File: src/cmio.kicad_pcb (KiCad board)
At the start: 2 copper layers, 7 parts, among them J1 CONN_02X20, J3 CM3Lite, J4 CONN_COAXIAL, J5 CONN_02X20, SW1 SW_Push

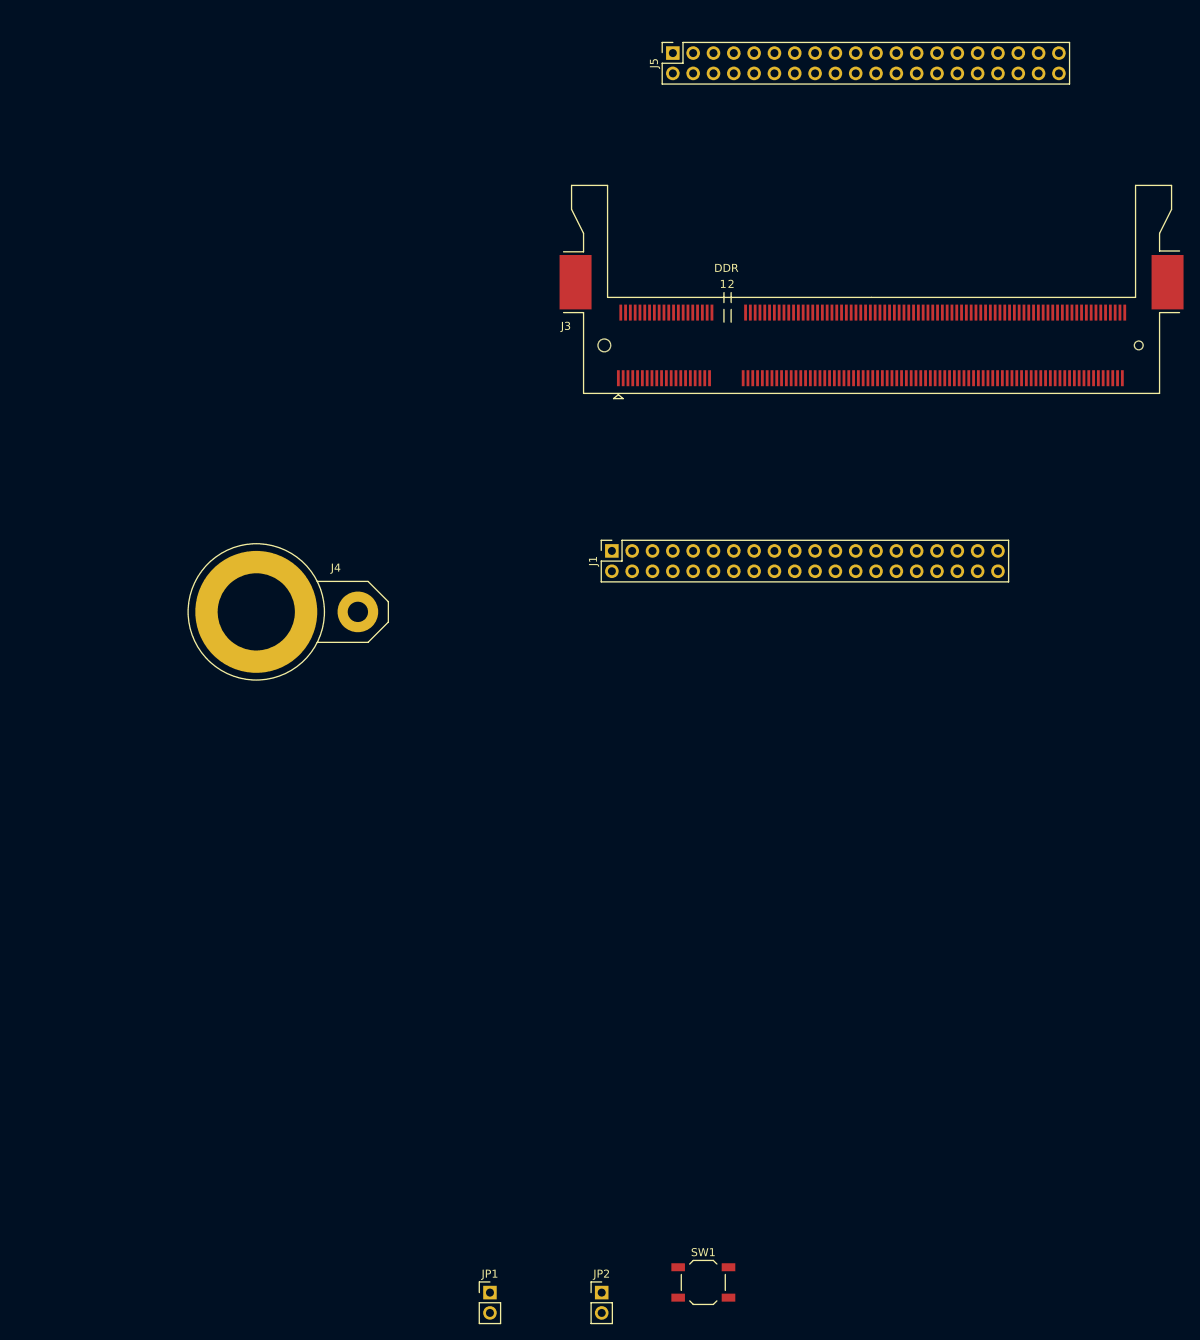
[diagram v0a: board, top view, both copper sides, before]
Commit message: Add Micro SD Card Footprint and 20-TQFP
Signed-off-by: Mahyar Koshkouei <deltabeard@users.noreply.github.com>
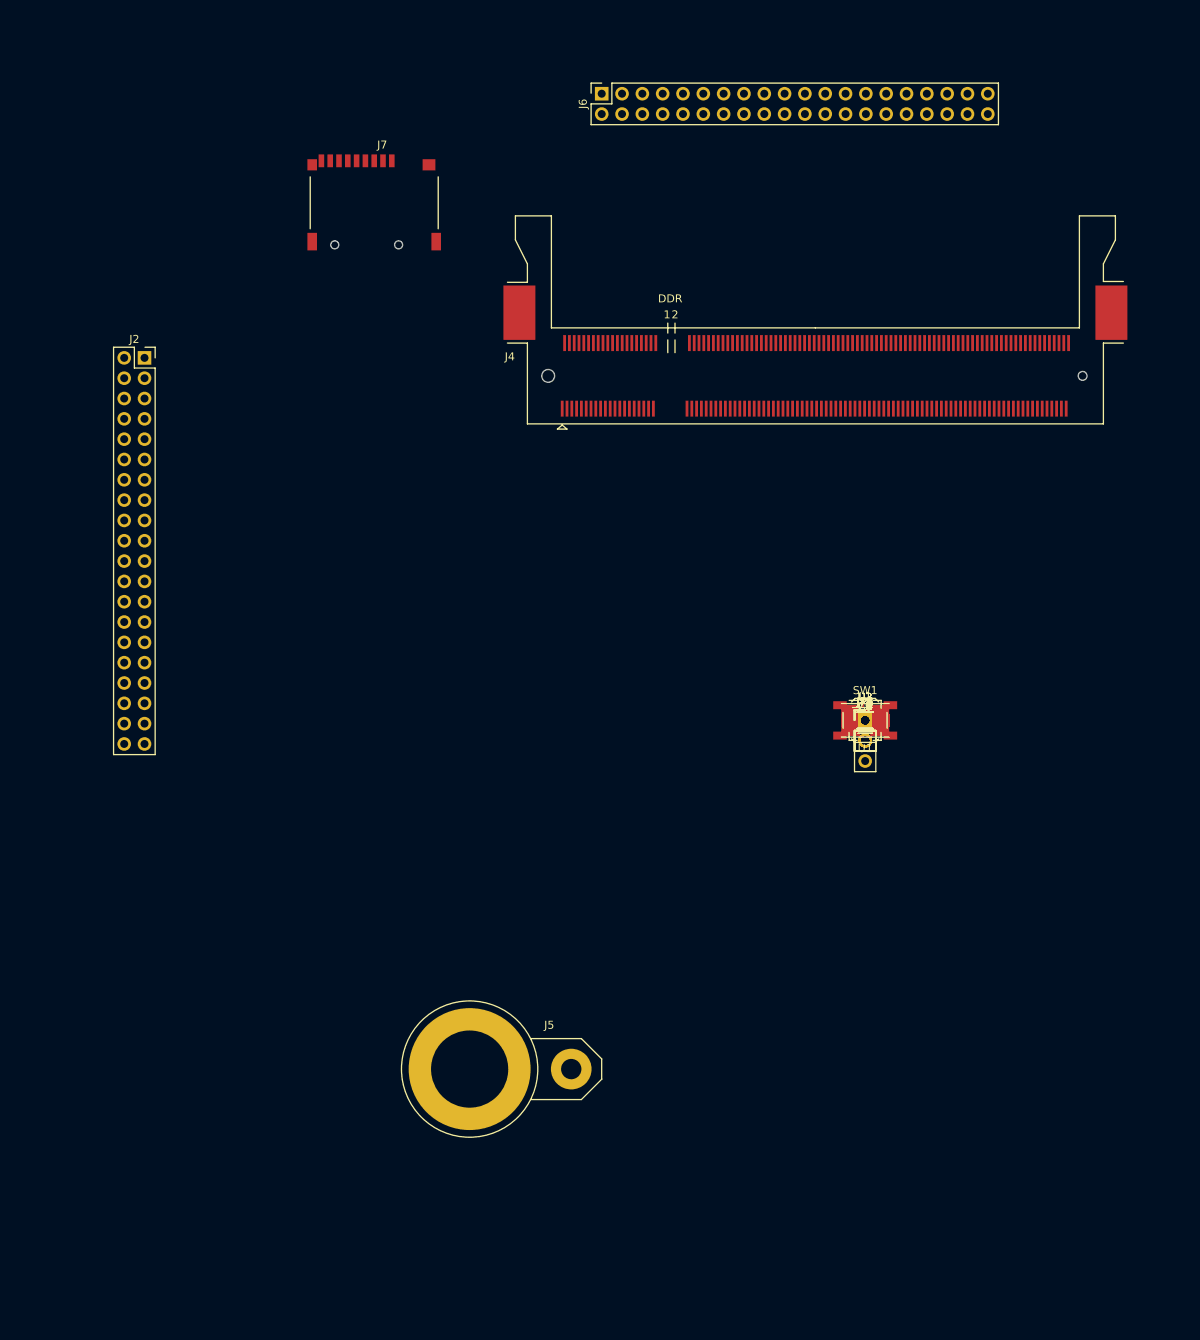
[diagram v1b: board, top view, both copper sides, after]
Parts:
- removed J3: CM3Lite, Sockets:Socket_SODIMM_DDR1-2_TE_1612618
- added C1, C2, C7, C8: 1uF, Capacitors_SMD:C_1206_HandSoldering, F.Cu at (148.5, 105.0)
- added C3, C6, C9: 22uF, Capacitors_SMD:C_1206_HandSoldering, F.Cu at (148.5, 105.0)
- added C4, C5: 10nF, Capacitors_SMD:C_1206_HandSoldering, F.Cu at (148.5, 105.0)
- added J2: CONN_02X20, Socket_Strips:Socket_Strip_Straight_2x20_Pitch2.54mm, F.Cu at (58.4, 59.7)
- added J6: CONN_02X20, Socket_Strips:Socket_Strip_Straight_2x20_Pitch2.54mm, F.Cu at (115.6, 26.7)
- added J7: Micro_SD_Card_TFP09_2_12B, foot:TFP09-2-12B, F.Cu at (87.1, 35.6)
- added JP3: 3.3 OUT, Pin_Headers:Pin_Header_Straight_1x02_Pitch2.54mm, F.Cu at (148.5, 105.0)
- added JP4: EN_Jumper, Socket_Strips:Socket_Strip_Straight_1x03_Pitch2.54mm, F.Cu at (148.5, 105.0)
- added JP5: TP, Pin_Headers:Pin_Header_Straight_1x02_Pitch2.54mm, F.Cu at (148.5, 105.0)
- added JP6: Disable SD Card, Pin_Headers:Pin_Header_Straight_1x02_Pitch2.54mm, F.Cu at (148.5, 105.0)
- added L1: 1uH, Inductors:Inductor_Taiyo-Yuden_NR-40xx_HandSoldering, F.Cu at (148.5, 105.0)
- added U1: ISL91107IR, foot:20_TQFP, F.Cu at (148.5, 105.0)
- added U2: LD3985M18R, TO_SOT_Packages_SMD:SOT-23-5, F.Cu at (148.5, 105.0)
- added U3: LD3985M28R, TO_SOT_Packages_SMD:SOT-23-5, F.Cu at (148.5, 105.0)
- J1: value CONN_02X20 -> CONN_01X02_MALE; footprint Socket_Strips:Socket_Strip_Straight_2x20_Pitch2.54mm -> Pin_Headers:Pin_Header_Straight_1x02_Pitch2.54mm
- J4: value CONN_COAXIAL -> CM3Lite; footprint Connect:BNC -> Sockets:Socket_SODIMM_DDR1-2_TE_1612618
- J5: value CONN_02X20 -> CONN_COAXIAL; footprint Socket_Strips:Socket_Strip_Straight_2x20_Pitch2.54mm -> Connect:BNC
- JP1: value TP -> 1V8 LDO IN
- JP2: value Disable SD Card -> 2V8 LDO IN
- moved J5 127.6 mm to (111.8, 148.6), turned to 0 degrees
- moved JP1 85.5 mm to (148.5, 105.0)
- moved JP2 78.7 mm to (148.5, 105.0)
- moved SW1 73.1 mm to (148.5, 105.0)
- moved J4 64.4 mm to (142.3, 61.9)
- moved J1 38.1 mm to (148.5, 105.0), turned to 0 degrees
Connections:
- J1 pad 2: +5V -> +3V3
- J4 pad 1: TVDAC -> GND
- J4 pad 2: GND -> Net-(J4-Pad2)
- J5 pad 1: +3V3 -> TVDAC
- J5 pad 2: +5V -> GND
- JP1 pad 1: (no net) -> +5V
- JP1 pad 2: +5V -> Net-(C1-Pad1)
- JP2 pad 1: Net-(J3-Pad2) -> +5V
- JP2 pad 2: GND -> Net-(C2-Pad1)
- SW1 pad 2: Net-(J3-Pad177) -> Net-(J4-Pad177)

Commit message: Before removing RPi GPIO Compat
Signed-off-by: Mahyar Koshkouei <deltabeard@users.noreply.github.com>
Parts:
- added J3: USB_OTG, foot:Micro_USB_B_10104110, F.Cu at (69.3, 24.0)
- added J8: CONN_01X06, Pin_Headers:Pin_Header_Straight_1x06_Pitch2.54mm, F.Cu at (66.0, 59.1)
- J4: footprint Sockets:Socket_SODIMM_DDR1-2_TE_1612618 -> foot:CM3_LeftDrillHole_Socket_SODIMM_DDR1-2_TE_1612618; moved to B.Cu
- J5: footprint Connect:BNC -> foot:RCA_PHONO
- moved JP4 133.2 mm to (45.7, 20.3), turned to 90 degrees
- moved JP3 131.6 mm to (45.7, 22.9), turned to 90 degrees
- moved JP5 129.6 mm to (45.7, 26.0), turned to 90 degrees
- moved JP1 128.1 mm to (45.7, 28.5), turned to 90 degrees
- moved JP2 126.6 mm to (45.7, 31.1), turned to 90 degrees
- moved J1 125.1 mm to (45.7, 33.6), turned to 90 degrees
- moved C2 112.7 mm to (57.0, 39.2), turned to 90 degrees
- moved L1 112.6 mm to (64.5, 30.0), turned to 270 degrees
- moved C8 111.6 mm to (61.8, 34.8)
- moved U3 110.1 mm to (60.2, 39.2)
- moved U1 109.1 mm to (69.6, 29.7)
- moved C5 106.9 mm to (64.0, 39.5), turned to 90 degrees
- moved C6 106.1 mm to (74.0, 29.5), turned to 90 degrees
- moved C3 105.1 mm to (71.0, 34.0)
- moved C9 104.3 mm to (76.5, 29.5), turned to 90 degrees
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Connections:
- J4 pad 165: (no net) -> /D+
- J4 pad 167: (no net) -> /D-
- J4 pad 168: (no net) -> OTDIG
- J6 pad 28: /DSI0_0 -> +5V
- J6 pad 30: /DSI0_1 -> +3V3
- J6 pad 32: /DSI0_2 -> +2V8
- J6 pad 34: /DSI0_3 -> +1V8
- J6 pad 36: /DSI0_4 -> GND
- J6 pad 38: /DSI0_5 -> GND
- JP5 pad 1: (no net) -> Net-(J3-Pad1)
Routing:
- net /D+: track 0.00 -> 47.4 mm, vias 0 -> 1
- net /D-: track 0.00 -> 47.1 mm, vias 0 -> 1
- net OTDIG: track 0.00 -> 42.9 mm, vias 0 -> 1
- net GND: track 0.00 -> 32.5 mm, vias 0 -> 3
- net G1: track 0.00 -> 31.4 mm
- net TVDAC: track 0.00 -> 25.7 mm
- net Net-(J3-Pad1): track 0.00 -> 24.6 mm, vias 0 -> 1
- net R1: track 0.00 -> 22.9 mm
- net G4: track 0.00 -> 22.1 mm
- net R0: track 0.00 -> 21.1 mm
- net G0: track 0.00 -> 20.6 mm
- net /DSI0_5: track 0.00 -> 20.6 mm
- net /DSI0_4: track 0.00 -> 18.1 mm
- net /DSI0_3: track 0.00 -> 17.1 mm
- net /DSI0_2: track 0.00 -> 14.8 mm
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- added copper zone on B.Cu, net GND
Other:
- board outline added: 89 x 51 mm
- rule via_min_size: 0.4 -> 0.5

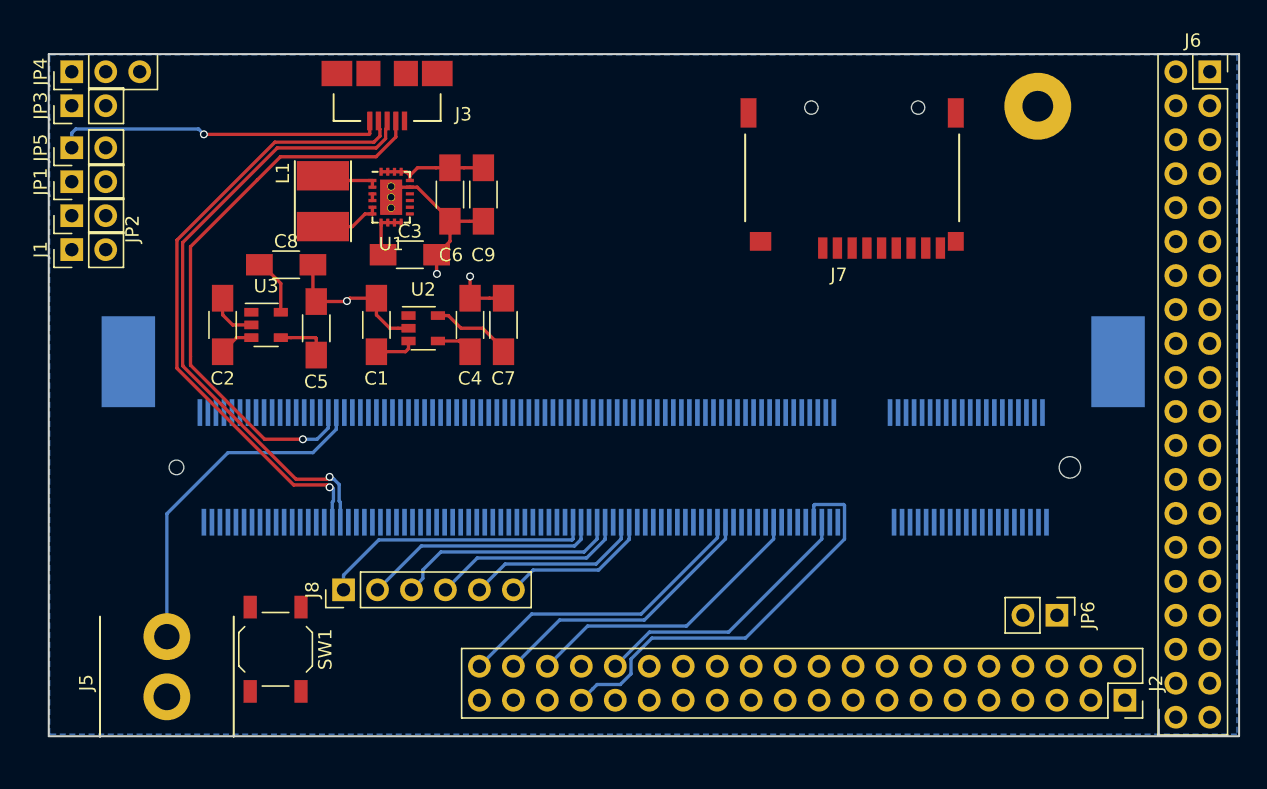
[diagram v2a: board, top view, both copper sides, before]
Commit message: Nearly finished routing
Remember to remove redundant GND tracks

Signed-off-by: Mahyar Koshkouei <deltabeard@users.noreply.github.com>
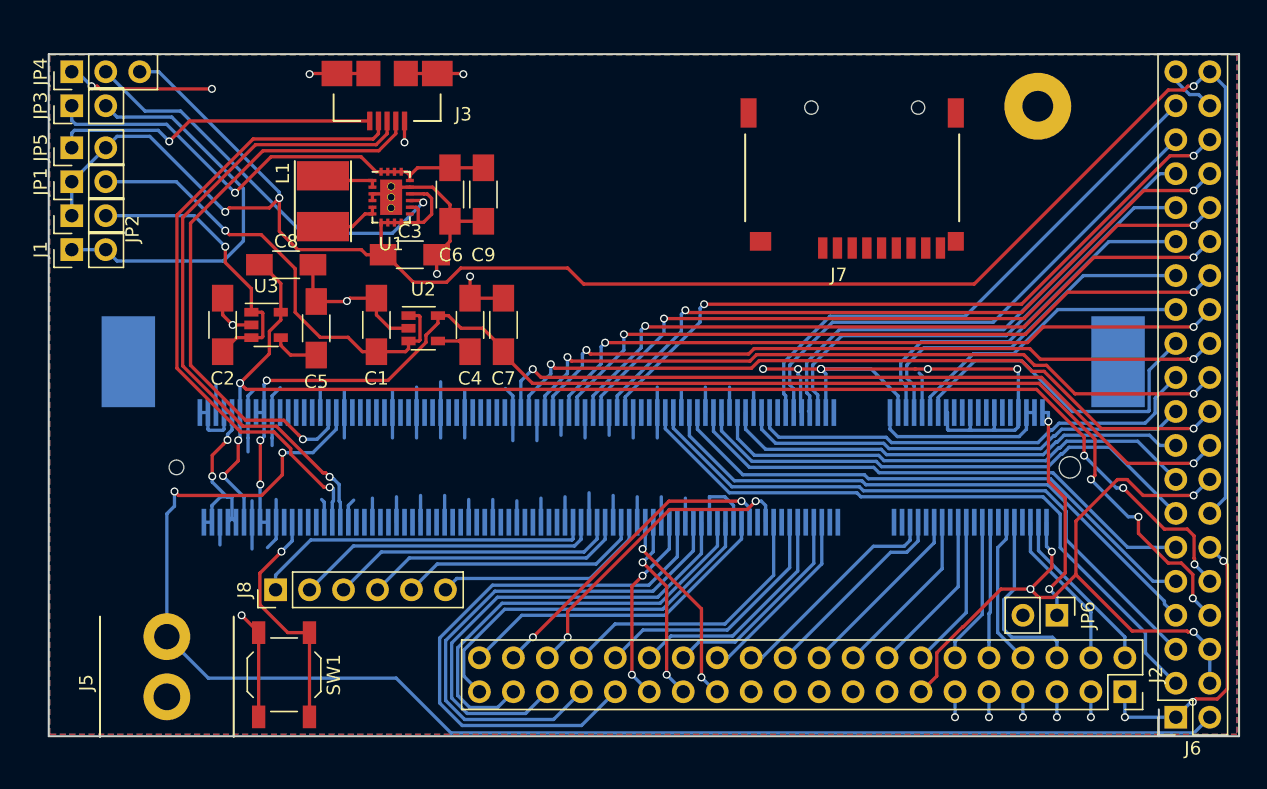
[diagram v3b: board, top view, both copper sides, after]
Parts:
- moved J6 48.3 mm to (128.3, 68.6), turned to 180 degrees
- moved J8 5.08 mm to (61.0, 59.1)
- moved SW1 2.01 mm to (61.6, 65.4)
- moved J2 0.64 mm to (124.5, 66.7)
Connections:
- J2 pad 10: G3 -> /G4
- J2 pad 11: G5 -> +3V3
- J2 pad 12: G6 -> /G5
- J2 pad 13: R7 -> GND
- J2 pad 14: GND -> /G6
- J2 pad 15: R2 -> GND
- J2 pad 16: R3 -> /G7
- J2 pad 17: +3V3 -> GND
- J2 pad 18: R4 -> /G8
- J2 pad 19: B6 -> GND
- J2 pad 2: +5V -> /G0
- J2 pad 20: GND -> /G9
- J2 pad 21: B5 -> GND
- J2 pad 22: R5 -> /G10
- J2 pad 23: B7 -> GND
- J2 pad 24: B4 -> /G11
- J2 pad 25: GND -> /G27
- J2 pad 26: B3 -> /G12
- J2 pad 27: PCLK -> /G26
- J2 pad 28: DE -> /G13
- J2 pad 29: B1 -> /G25
- J2 pad 3: VSYNC -> +3V3
- J2 pad 30: GND -> /G14
- J2 pad 31: B2 -> /G24
- J2 pad 32: G0 -> /G15
- J2 pad 33: G1 -> /G23
- J2 pad 34: GND -> /G16
- J2 pad 35: G7 -> /G22
- J2 pad 36: G4 -> /G17
- J2 pad 37: R6 -> /G21
- J2 pad 38: R0 -> /G18
- J2 pad 39: GND -> /G20
- J2 pad 4: +5V -> /G1
- J2 pad 40: R1 -> /G19
- J2 pad 5: HSYNC -> +3V3
- J2 pad 6: GND -> /G2
- J2 pad 7: B0 -> +3V3
- J2 pad 8: G2 -> /G3
- J2 pad 9: GND -> +3V3
- J4 pad 11: HSYNC -> /G3
- J4 pad 15: B0 -> /G4
- J4 pad 17: B1 -> /G5
- J4 pad 21: B2 -> /G6
- J4 pad 23: B3 -> /G7
- J4 pad 27: B4 -> /G8
- J4 pad 29: B5 -> /G9
- J4 pad 3: PCLK -> /G0
- J4 pad 33: B6 -> /G10
- J4 pad 35: B7 -> /G11
- J4 pad 45: G0 -> /G12
- J4 pad 47: G1 -> /G13
- J4 pad 5: DE -> /G1
- J4 pad 51: G2 -> /G14
- J4 pad 53: G3 -> /G15
- J4 pad 57: G4 -> /G16
- J4 pad 59: G5 -> /G17
- J4 pad 63: G6 -> /G18
- J4 pad 65: G7 -> /G19
- J4 pad 69: R0 -> /G20
- J4 pad 71: R1 -> /G21
- J4 pad 75: R2 -> /G22
- J4 pad 77: R3 -> /G23
- J4 pad 81: R4 -> /G24
- J4 pad 83: R5 -> /G25
- J4 pad 87: R6 -> /G26
- J4 pad 89: R7 -> /G27
- J4 pad 9: VSYNC -> /G2
- J6 pad 10: /DSI1_2 -> +2V8
- J6 pad 11: /G31 -> /G41
- J6 pad 12: /DSI1_3 -> +3V3
- J6 pad 13: /G32 -> /G40
- J6 pad 14: /DSI1_4 -> +5V
- J6 pad 15: /G33 -> /G39
- J6 pad 16: /DSI1_5 -> GND
- J6 pad 17: /G34 -> /G38
- J6 pad 18: /DSI1_6 -> /DSI1_9
- J6 pad 19: /G35 -> /G37
- J6 pad 2: +5V -> TVDAC
- J6 pad 20: /DSI1_7 -> /DSI1_8
- J6 pad 22: /DSI1_8 -> /DSI1_7
- J6 pad 23: /G37 -> /G28
- J6 pad 24: /DSI1_9 -> /DSI1_6
- J6 pad 25: /G38 -> /G29
- J6 pad 26: GND -> /DSI1_5
- J6 pad 27: /G39 -> /G30
- J6 pad 28: +5V -> /DSI1_4
- J6 pad 29: /G40 -> /G31
- J6 pad 3: GND -> /G45
- J6 pad 30: +3V3 -> /DSI1_3
- J6 pad 31: /G41 -> /G32
- J6 pad 32: +2V8 -> /DSI1_2
- J6 pad 33: /G42 -> /G33
- J6 pad 34: +1V8 -> /DSI1_1
- J6 pad 35: /G43 -> /G34
- J6 pad 36: GND -> /DSI1_0
- J6 pad 37: /G44 -> /G35
- J6 pad 39: /G45 -> GND
- J6 pad 40: TVDAC -> +5V
- J6 pad 5: /G28 -> /G44
- J6 pad 6: /DSI1_0 -> GND
- J6 pad 7: /G29 -> /G43
- J6 pad 8: /DSI1_1 -> +1V8
- J6 pad 9: /G30 -> /G42
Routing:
- net GND: track 32.5 -> 273.2 mm, vias 3 -> 20
- net +5V: track 3.97 -> 163.1 mm, vias 0 -> 3
- net +2V8: track 4.33 -> 103.2 mm, vias 0 -> 6
- net +3V3: track 0.00 -> 94.2 mm, vias 0 -> 10
- net +1V8: track 6.14 -> 98.6 mm, vias 0 -> 6
- net TVDAC: track 25.7 -> 109.2 mm, vias 0 -> 2
- net /DSI1_9: track 0.00 -> 57.8 mm, vias 0 -> 2
- net /DSI1_8: track 0.00 -> 56.6 mm, vias 0 -> 2
- net /DSI1_7: track 0.00 -> 54.9 mm, vias 0 -> 2
- net /DSI1_0: track 0.00 -> 53.4 mm, vias 0 -> 2
- net /DSI1_6: track 0.00 -> 53.4 mm, vias 0 -> 2
- net /DSI1_1: track 0.00 -> 53.4 mm, vias 0 -> 2
- net /DSI1_2: track 0.00 -> 53.3 mm, vias 0 -> 2
- net /DSI1_3: track 0.00 -> 53.0 mm, vias 0 -> 2
- net /DSI1_4: track 0.00 -> 52.9 mm, vias 0 -> 2
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- added copper zone on F.Cu, net +3V3

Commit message: Final Checks
Signed-off-by: Mahyar Koshkouei <deltabeard@users.noreply.github.com>
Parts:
- added J9: USB_OTG, foot:Micro_USB_B_10104110, F.Cu at (49.3, 52.5)
- added JP7: PWRUSB, Pin_Headers:Pin_Header_Straight_1x02_Pitch2.54mm, F.Cu at (45.7, 42.7)
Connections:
- J3 pad 2: /D- -> (no net)
- J3 pad 3: /D+ -> (no net)
- J3 pad 4: OTDIG -> (no net)
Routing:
- net GND: track 273.2 -> 341.8 mm, vias 20 -> 24
- net DAT2: track 0.00 -> 30.3 mm, vias 0 -> 1
- net DAT3: track 0.00 -> 29.8 mm, vias 0 -> 1
- net CMD: track 0.00 -> 29.0 mm, vias 0 -> 1
- net CLK: track 0.00 -> 28.0 mm, vias 0 -> 1
- net /D-: track 48.2 -> 20.4 mm
- net /D+: track 48.1 -> 20.4 mm
- net DAT0: track 0.00 -> 27.0 mm, vias 0 -> 1
- net DAT1: track 0.00 -> 26.7 mm, vias 0 -> 1
- net +5V: track 163.1 -> 187.9 mm
- net OTDIG: track 43.8 -> 19.1 mm
- net Net-(J9-Pad1): track 0.00 -> 13.2 mm, vias 0 -> 1
- net +3V3: track 94.2 -> 82.0 mm, vias 10 -> 18
- net /DSI1_0: track 53.4 -> 64.1 mm
- net /DSI1_1: track 53.4 -> 62.8 mm
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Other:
- board text added: "Compute Module IO Board V1 Mahyar Koshkouei"
- board text added: "Micro SD Card"
- board text added: "USB"
- board text added: "USB Power Switch"
